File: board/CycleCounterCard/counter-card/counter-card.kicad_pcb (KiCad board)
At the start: 4 copper layers, 106.7 x 105.4 mm, 33 parts, among them J1 Bus_Hydra_8bit, J2 74F86, J3 74F86, J4 74F86, J5 74F86, U1 74F191, U10 74F191, U11 74F191, U12 74F573, U13 74F573, U14 74F191, U15 74F191, U16 74F191, U17 74F191, U18 74F573, U19 74F573, U2 74F573, U21 74F573, U22 74F191, U24 74F02, U26 74F573, U27 74F00, U3 74F138, U4 74F191, U6 74F573, U7 74F191, U8 74F191, U9 74F191

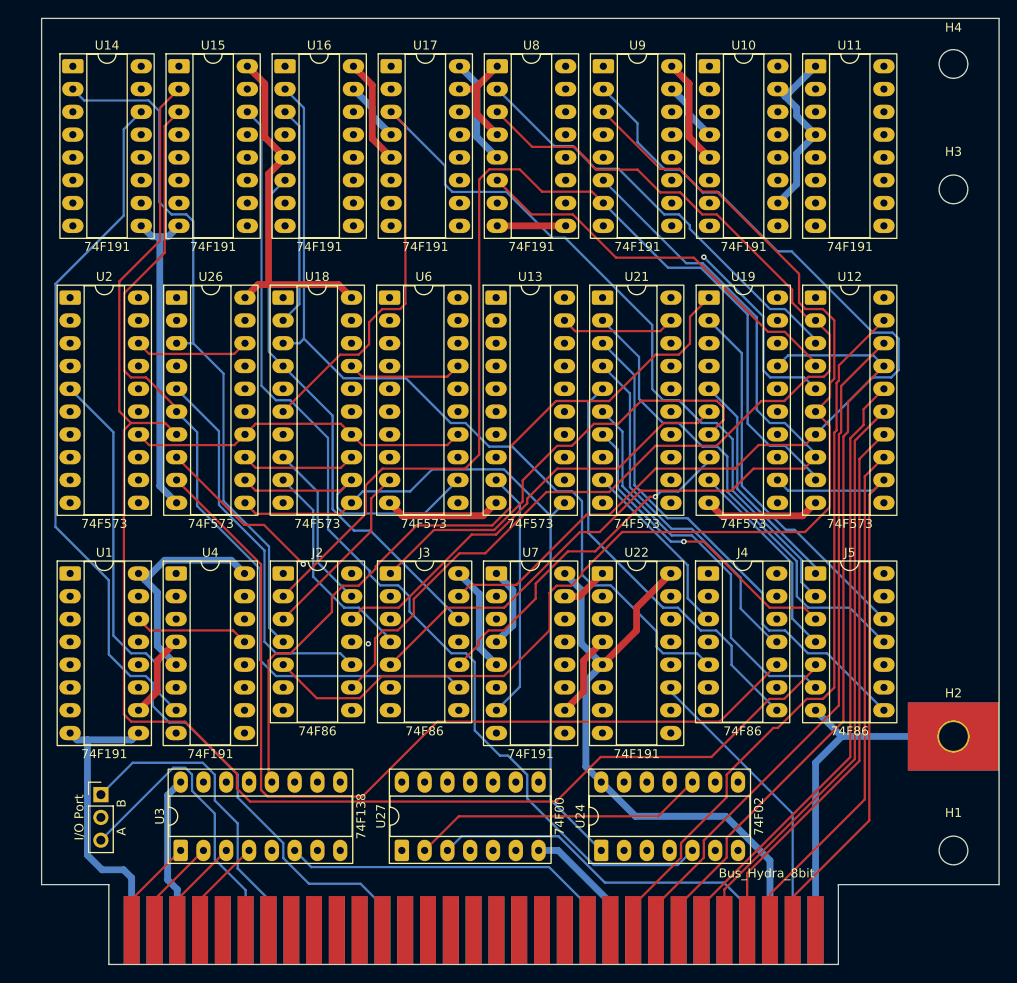
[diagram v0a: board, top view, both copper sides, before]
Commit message: V2.0: wait states, GAL glue logic, serial clock and review fixes
Main board schematic:
- Replace the T4-T7 clock divider with RDY wait states. Fixed 7.16 MHz
  CPU clock; J36 selects 3.58 MHz for Rockwell parts. Waits are set per
  region through the write-only register at $FFF5 (reset = 3 waits).
- Move address decode, strobes, the wait-state generator, the IRQ
  encoder/latch/vector mux, ROM bank gating and DMA sync into seven GALs
  (U81-U86 ATF22V10C, U87 ATF16V8C), removing 29 ICs. CUPL sources,
  JEDECs and notes are in board/PLDs/V2.
- 1.8432 MHz serial clock, soft-power latch, -5V regulator, bulk caps,
  pull-ups, audio coupling/decoupling, GNDA tie, read-only Z register
  and other design-review fixes.
- New WaitStates and Support sheets; project symbol library
  hydra16.kicad_sym with sym-lib-table.

PCB updated from the schematic. Includes pending changes to the counter,
bus breakout and memory daughter card projects.

Firmware:
- Remove S_REGISTER; T/U/V/W now at $FFF0-$FFF3 to match the hardware.
- Add math.s and sound.s (included by os_main.s).
- Rebuild the 65C02 ROM image.

Co-Authored-By: Claude Opus 5.5 <noreply@anthropic.com>
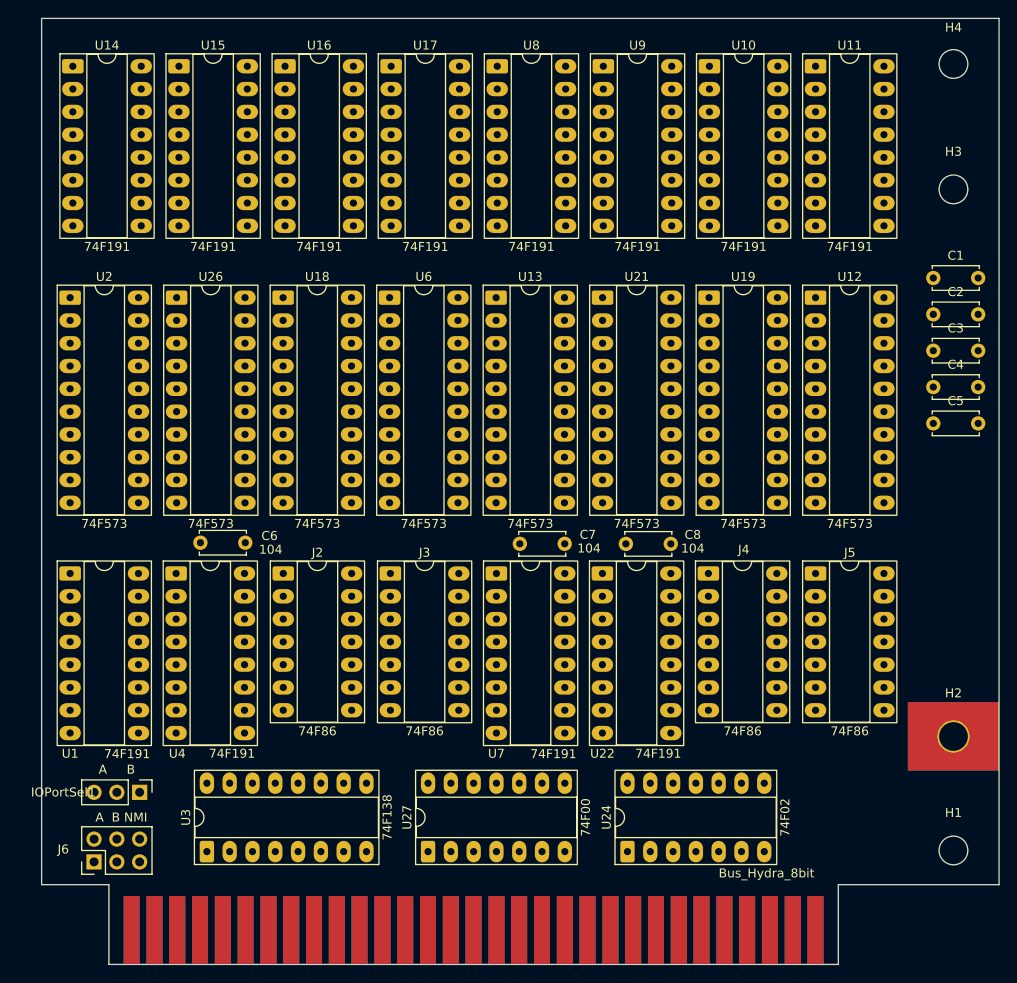
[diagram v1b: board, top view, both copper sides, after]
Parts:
- added C1: 104, Capacitor_THT:C_Disc_D5.0mm_W2.5mm_P5.00mm, F.Cu at (176.4, 72.6)
- added C2: 104, Capacitor_THT:C_Disc_D5.0mm_W2.5mm_P5.00mm, F.Cu at (176.4, 76.7)
- added C3: 104, Capacitor_THT:C_Disc_D5.0mm_W2.5mm_P5.00mm, F.Cu at (176.4, 80.7)
- added C4: 104, Capacitor_THT:C_Disc_D5.0mm_W2.5mm_P5.00mm, F.Cu at (176.4, 84.8)
- added C5: 104, Capacitor_THT:C_Disc_D5.0mm_W2.5mm_P5.00mm, F.Cu at (176.4, 88.8)
- added C6: 104, Capacitor_THT:C_Disc_D5.0mm_W2.5mm_P5.00mm, F.Cu at (94.8, 102.1)
- added C7: 104, Capacitor_THT:C_Disc_D5.0mm_W2.5mm_P5.00mm, F.Cu at (130.4, 102.2)
- added C8: 104, Capacitor_THT:C_Disc_D5.0mm_W2.5mm_P5.00mm, F.Cu at (142.2, 102.2)
- added J6: Conn_02x03_Odd_Even, Connector_PinHeader_2.54mm:PinHeader_2x03_P2.54mm_Vertical, F.Cu at (82.9, 137.7)
- IOPortSel1: renamed from I/O Port; value A B -> Conn_01x03_Pin
- moved IOPortSel1 4.33 mm to (88.0, 129.9), turned to -90 degrees
- moved U27 2.92 mm to (120.1, 136.5)
- moved U3 2.92 mm to (95.5, 136.5)
- moved U24 2.92 mm to (142.4, 136.5)
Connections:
- J1 pad 37: unconnected-(J1-PHI1O-Pad37) -> PHI1O
- U24 pad 3: OE0_S -> PHI1O
- U27 pad 3: NMIB -> Net-(J6-Pin_1)
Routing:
- net GND: track 701.5 -> 0.00 mm
- net +5V: track 567.9 -> 0.00 mm
- net RESB: track 241.6 -> 0.00 mm
- net D0: track 170.8 -> 0.00 mm
- net Q5: track 167.5 -> 0.00 mm
- net D1: track 165.9 -> 0.00 mm
- net D2: track 162.3 -> 0.00 mm
- net Q8: track 159.5 -> 0.00 mm
- net D3: track 158.7 -> 0.00 mm
- net Q2: track 157.1 -> 0.00 mm
- net D4: track 155.1 -> 0.00 mm
- net D5: track 151.5 -> 0.00 mm
- net D7: track 150.5 -> 0.00 mm
- net RC1: track 149.5 -> 0.00 mm
- net D6: track 147.9 -> 0.00 mm
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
